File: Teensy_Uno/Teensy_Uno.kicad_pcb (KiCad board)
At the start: 2 copper layers, 138.4 x 67.3 mm, 30 parts, among them P1 Power, P10 CONN_01X13, P10a1 CONN_01X10, P11 CONN_01X24, P12 CONN_01X24, P13 CONN_01X05, P14 CONN_01X03, P15 CONN_01X03, P16 CONN_01X01, P17 CONN_01X24, P18 CONN_01X02, P19 CONN_01X24, P1a1 CONN_01X09, P2 Analog, P20 CONN_01X13, P21 CONN_01X13, P2a1 CONN_01X09, P3 Digital, P4 Digital, P5 CONN_01X01, P6 CONN_01X01, P7 CONN_01X01, P8 CONN_01X01, P9 CONN_01X13, P9a1 CONN_01X09, SW1 SW_PUSH_SMALL_H, SW2 SW_PUSH_SMALL_H

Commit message: fixed connection issues
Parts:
- moved P13 10.2 mm to (103.4, 95.9), turned to 270 degrees
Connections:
- net /2 renamed Net-(P11-Pad4)
- P11 pad 14: Net-(P11-Pad14) -> /12(MISO)
- P12 pad 14: Net-(P11-Pad14) -> /12(MISO)
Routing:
- net /12(MISO): track 0.00 -> 92.6 mm, vias 0 -> 1
- net Net-(P13-Pad1): track 45.6 -> 35.4 mm
- net Net-(P11-Pad14): track 7.62 -> 0.00 mm
- net Net-(BT1-Pad1): track 75.0 -> 81.2 mm
- net Net-(P13-Pad2): track 41.8 -> 37.8 mm
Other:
- board text added: "PGM"
- board text added: "RST"

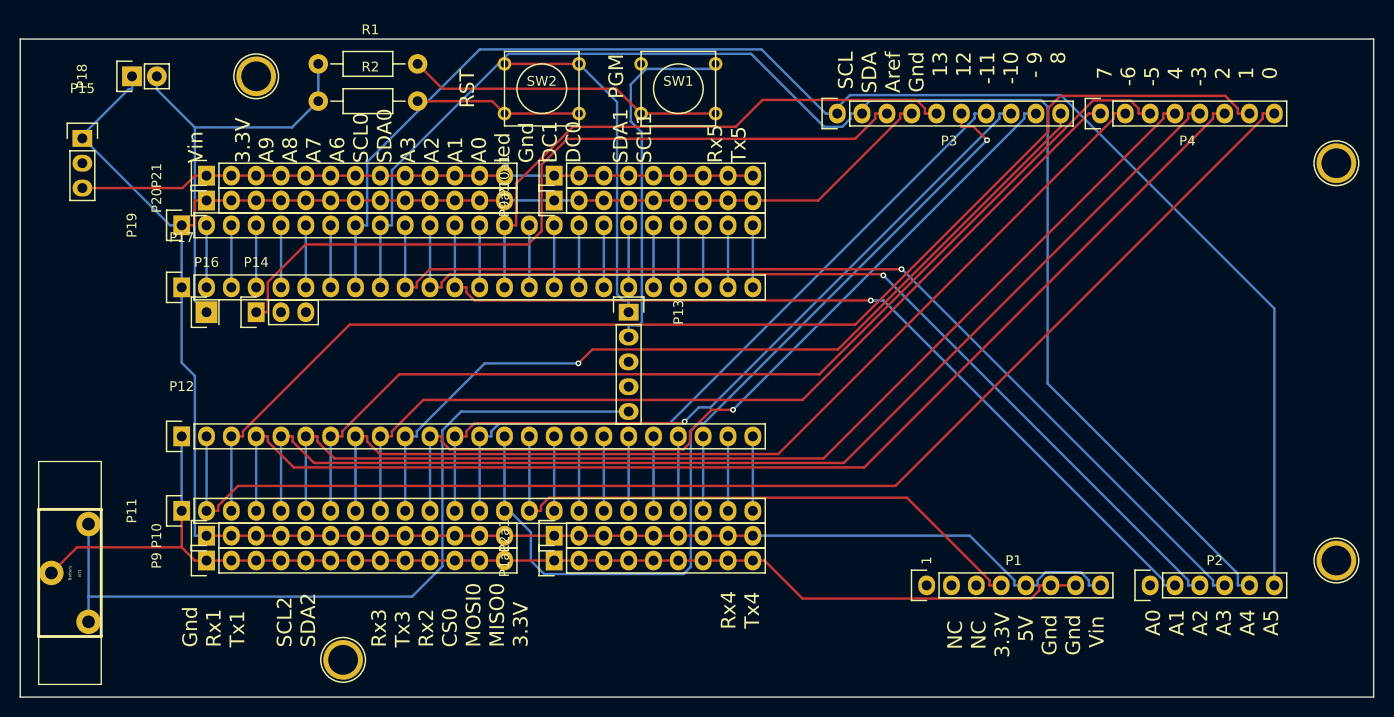
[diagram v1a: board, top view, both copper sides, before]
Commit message: corrected reset voltage to 3.3v
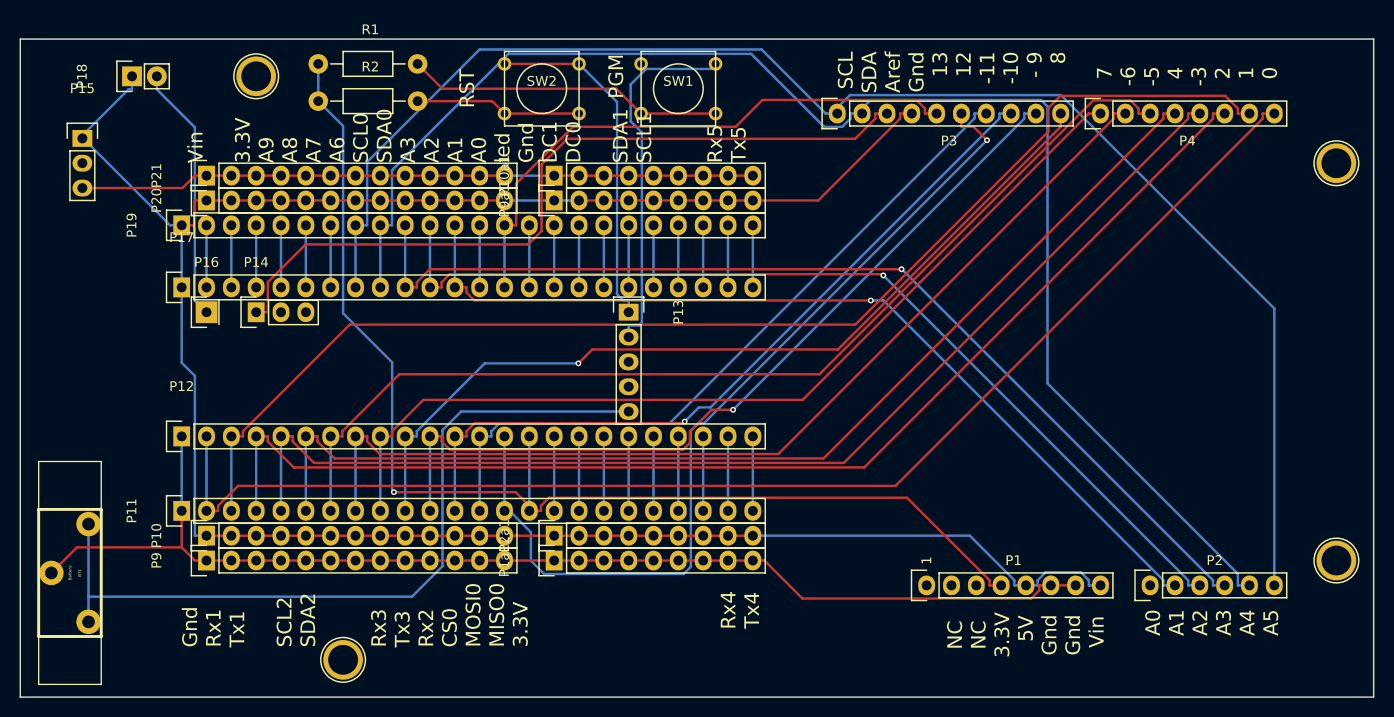
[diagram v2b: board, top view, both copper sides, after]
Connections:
- R1 pad 1: Net-(P16-Pad1) -> Net-(P1-Pad4)
- R2 pad 1: Net-(P16-Pad1) -> Net-(P1-Pad4)
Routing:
- net Net-(P1-Pad4): track 60.8 -> 122.9 mm, vias 0 -> 1
- net Net-(P16-Pad1): track 43.8 -> 26.2 mm

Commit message: Additional corrections
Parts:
- removed R1, R2: 10k, Resistors_ThroughHole:Resistor_Horizontal_RM10mm
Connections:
- P10a1 pad 1: Net-(P10a1-Pad1) -> Net-(BT1-Pad2)
- P10a1 pad 2: Net-(P10a1-Pad1) -> Net-(BT1-Pad2)
- P10a1 pad 3: Net-(P10a1-Pad1) -> Net-(BT1-Pad2)
- P10a1 pad 4: Net-(P10a1-Pad1) -> Net-(BT1-Pad2)
- P10a1 pad 5: Net-(P10a1-Pad1) -> Net-(BT1-Pad2)
- P10a1 pad 6: Net-(P10a1-Pad1) -> Net-(BT1-Pad2)
- P10a1 pad 7: Net-(P10a1-Pad1) -> Net-(BT1-Pad2)
- P10a1 pad 8: Net-(P10a1-Pad1) -> Net-(BT1-Pad2)
- P10a1 pad 9: Net-(P10a1-Pad1) -> Net-(BT1-Pad2)
- P12 pad 15: Net-(P1-Pad4) -> Net-(P12-Pad15)
- P15 pad 3: Net-(P10a1-Pad1) -> Net-(BT1-Pad2)
- P17 pad 13: Net-(P17-Pad13) -> /A0
- P19 pad 13: Net-(P17-Pad13) -> /A0
- P21 pad 1: Net-(P10a1-Pad1) -> Net-(BT1-Pad2)
- P21 pad 10: Net-(P10a1-Pad1) -> Net-(BT1-Pad2)
- P21 pad 11: Net-(P10a1-Pad1) -> Net-(BT1-Pad2)
- P21 pad 12: Net-(P10a1-Pad1) -> Net-(BT1-Pad2)
- P21 pad 13: Net-(P10a1-Pad1) -> Net-(BT1-Pad2)
- P21 pad 2: Net-(P10a1-Pad1) -> Net-(BT1-Pad2)
- P21 pad 3: Net-(P10a1-Pad1) -> Net-(BT1-Pad2)
- P21 pad 4: Net-(P10a1-Pad1) -> Net-(BT1-Pad2)
- P21 pad 5: Net-(P10a1-Pad1) -> Net-(BT1-Pad2)
- P21 pad 6: Net-(P10a1-Pad1) -> Net-(BT1-Pad2)
- P21 pad 7: Net-(P10a1-Pad1) -> Net-(BT1-Pad2)
- P21 pad 8: Net-(P10a1-Pad1) -> Net-(BT1-Pad2)
- P21 pad 9: Net-(P10a1-Pad1) -> Net-(BT1-Pad2)
- SW1 pad 2: Net-(R1-Pad2) -> Net-(BT1-Pad2)
- SW2 pad 2: Net-(R2-Pad2) -> Net-(BT1-Pad2)
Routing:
- net Net-(BT1-Pad2): track 120.2 -> 241.8 mm
- net /A0: track 0.00 -> 111.3 mm, vias 0 -> 5
- net Net-(P1-Pad4): track 122.9 -> 53.1 mm, vias 1 -> 0
- net Net-(P10a1-Pad1): track 69.1 -> 0.00 mm
- net Net-(R1-Pad2): track 32.6 -> 0.00 mm
- net Net-(R2-Pad2): track 17.0 -> 0.00 mm
- net Net-(P12-Pad15): track 0.00 -> 7.62 mm
- net Net-(P17-Pad13): track 6.35 -> 0.00 mm
- net Net-(P17-Pad9): track 148.7 -> 149.6 mm

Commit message: Final updates and corrections
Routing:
- net Net-(BT1-Pad2): track 241.8 -> 248.2 mm
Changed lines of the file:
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@@
     (thickness 1.6)
     (drawings 14)
-    (tracks 439)
+    (tracks 440)
     (zones 0)
     (modules 28)
@@
   (segment (start 48.1279 124.978) (end 48.1279 127.556) (width 0.25) (layer B.Cu) (net 23))
   (segment (start 48.1279 127.556) (end 48.1279 127.5563) (width 0.25) (layer B.Cu) (net 23))
+  (segment (start 90.678 75.565) (end 90.678 81.915) (width 0.25) (layer F.Cu) (net 24))
   (segment (start 98.298 75.565) (end 99.285828 75.565) (width 0.25) (layer F.Cu) (net 24))
   (segment (start 99.285828 75.565) (end 104.648 75.565) (width 0.25) (layer F.Cu) (net 24))

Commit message: update
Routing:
- net Net-(P17-Pad9): track 149.6 -> 147.3 mm, vias 0 -> 2
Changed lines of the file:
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@@
   (general
     (links 179)
-    (no_connects 1)
+    (no_connects 0)
     (area 41.072999 66.721666 180.801334 135.330001)
     (thickness 1.6)
@@
   (segment (start 65.278 118.745) (end 62.738 118.745) (width 0.25) (layer F.Cu) (net 27))
   (segment (start 62.738 118.745) (end 60.198 118.745) (width 0.25) (layer F.Cu) (net 27))
+  (segment (start 115.57 72.517) (end 120.396 77.343) (width 0.25) (layer B.Cu) (net 28))
+  (segment (start 120.396 77.343) (end 125.6284 77.343) (width 0.25) (layer B.Cu) (net 28))
+  (segment (start 125.6284 77.343) (end 127.254 75.7174) (width 0.25) (layer B.Cu) (net 28))
+  (segment (start 127.254 75.7174) (end 127.254 75.565) (width 0.25) (layer B.Cu) (net 28))
+  (via (at 115.57 72.517) (size 0.6) (drill 0.4) (layers F.Cu B.Cu) (net 28))
+  (segment (start 94.488 72.517) (end 115.57 72.517) (width 0.25) (layer F.Cu) (net 28))
+  (via (at 94.488 72.517) (size 0.6) (drill 0.4) (layers F.Cu B.Cu) (net 28))
+  (segment (start 87.63 72.517) (end 94.488 72.517) (width 0.25) (layer B.Cu) (net 28))
   (segment (start 166.878 123.825) (end 165.689 123.825) (width 0.25) (layer B.Cu) (net 28))
   (segment (start 165.689 122.636) (end 146.225 103.172) (width 0.25) (layer B.Cu) (net 28))
@@
   (segment (start 77.978 86.995) (end 79.1669 86.995) (width 0.25) (layer B.Cu) (net 28))
   (segment (start 79.1669 86.995) (end 79.1669 80.9801) (width 0.25) (layer B.Cu) (net 28))
-  (segment (start 87.63 72.517) (end 91.948 72.517) (width 0.25) (layer B.Cu) (net 28))
   (segment (start 79.1669 80.9801) (end 87.63 72.517) (width 0.25) (layer B.Cu) (net 28))
-  (segment (start 91.948 72.517) (end 95.003501 69.461499) (width 0.25) (layer B.Cu) (net 28))
-  (segment (start 95.003501 69.461499) (end 115.308499 69.461499) (width 0.25) (layer B.Cu) (net 28))
-  (segment (start 115.308499 69.461499) (end 122.936 77.089) (width 0.25) (layer B.Cu) (net 28))
-  (segment (start 127.254 75.7174) (end 127.254 75.565) (width 0.25) (layer B.Cu) (net 28))
-  (segment (start 122.936 77.089) (end 125.8824 77.089) (width 0.25) (layer B.Cu) (net 28))
-  (segment (start 125.8824 77.089) (end 127.254 75.7174) (width 0.25) (layer B.Cu) (net 28))
   (segment (start 77.978 93.345) (end 77.978 86.995) (width 0.25) (layer B.Cu) (net 28))
   (segment (start 126.742 75.565) (end 127.254 75.565) (width 0.25) (layer B.Cu) (net 28))
@@
   (segment (start 103.378 94.6961) (end 102.858 94.6961) (width 0.25) (layer B.Cu) (net 42))
   (segment (start 103.378 95.885) (end 103.378 94.6961) (width 0.25) (layer B.Cu) (net 42))
-  (segment (start 104.648 70.485) (end 105.165 71.0017) (width 0.25) (layer B.Cu) (net 43))
-  (segment (start 111.751 71.0017) (end 112.268 70.485) (width 0.25) (layer B.Cu) (net 43))
-  (segment (start 105.165 71.0017) (end 111.751 71.0017) (width 0.25) (layer B.Cu) (net 43))
-  (segment (start 103.588 72.5783) (end 105.165 71.0017) (width 0.25) (layer B.Cu) (net 43))
-  (segment (start 103.588 76.3714) (end 103.588 72.5783) (width 0.25) (layer B.Cu) (net 43))
-  (segment (start 104.729 77.512) (end 103.588 76.3714) (width 0.25) (layer B.Cu) (net 43))
+  (segment (start 104.648 70.485) (end 105.635828 70.485) (width 0.25) (layer B.Cu) (net 43))
+  (segment (start 105.635828 70.485) (end 112.268 70.485) (width 0.25) (layer B.Cu) (net 43))
+  (segment (start 103.378 98.425) (end 103.378 97.2361) (width 0.25) (layer B.Cu) (net 43))
+  (segment (start 103.378 97.2361) (end 104.418 97.2361) (width 0.25) (layer B.Cu) (net 43))
   (segment (start 104.729 96.9254) (end 104.729 77.512) (width 0.25) (layer B.Cu) (net 43))
   (segment (start 104.418 97.2361) (end 104.729 96.9254) (width 0.25) (layer B.Cu) (net 43))
-  (segment (start 103.378 97.2361) (end 104.418 97.2361) (width 0.25) (layer B.Cu) (net 43))
-  (segment (start 103.378 98.425) (end 103.378 97.2361) (width 0.25) (layer B.Cu) (net 43))
+  (segment (start 104.729 77.512) (end 103.588 76.3714) (width 0.25) (layer B.Cu) (net 43))
+  (segment (start 103.588 76.3714) (end 103.588 71.545) (width 0.25) (layer B.Cu) (net 43))
+  (segment (start 103.588 71.545) (end 104.648 70.485) (width 0.25) (layer B.Cu) (net 43))
   (segment (start 66.4669 95.885) (end 65.278 95.885) (width 0.25) (layer F.Cu) (net 46))
   (segment (start 66.4669 92.8191) (end 66.4669 95.885) (width 0.25) (layer F.Cu) (net 46))
